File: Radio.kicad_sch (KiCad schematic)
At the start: 3 parts, among them U4 X1000, U5 AP6212

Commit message: Update (Display)
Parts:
- U4: footprint (none) -> TheBrutzlers_Lib:BGA256C80P16X16_1300X1300X130N
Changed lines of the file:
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@@
     (property "Reference" "U4" (id 0) (at 149.86 78.74 0))
     (property "Value" "X1000" (id 1) (at 149.86 81.28 0))
-    (property "Footprint" "" (id 2) (at 153.67 95.25 0)
+    (property "Footprint" "TheBrutzlers_Lib:BGA256C80P16X16_1300X1300X130N" (id 2) (at 153.67 95.25 0)
       (effects (font (size 1.27 1.27)) (justify left) hide)
     )

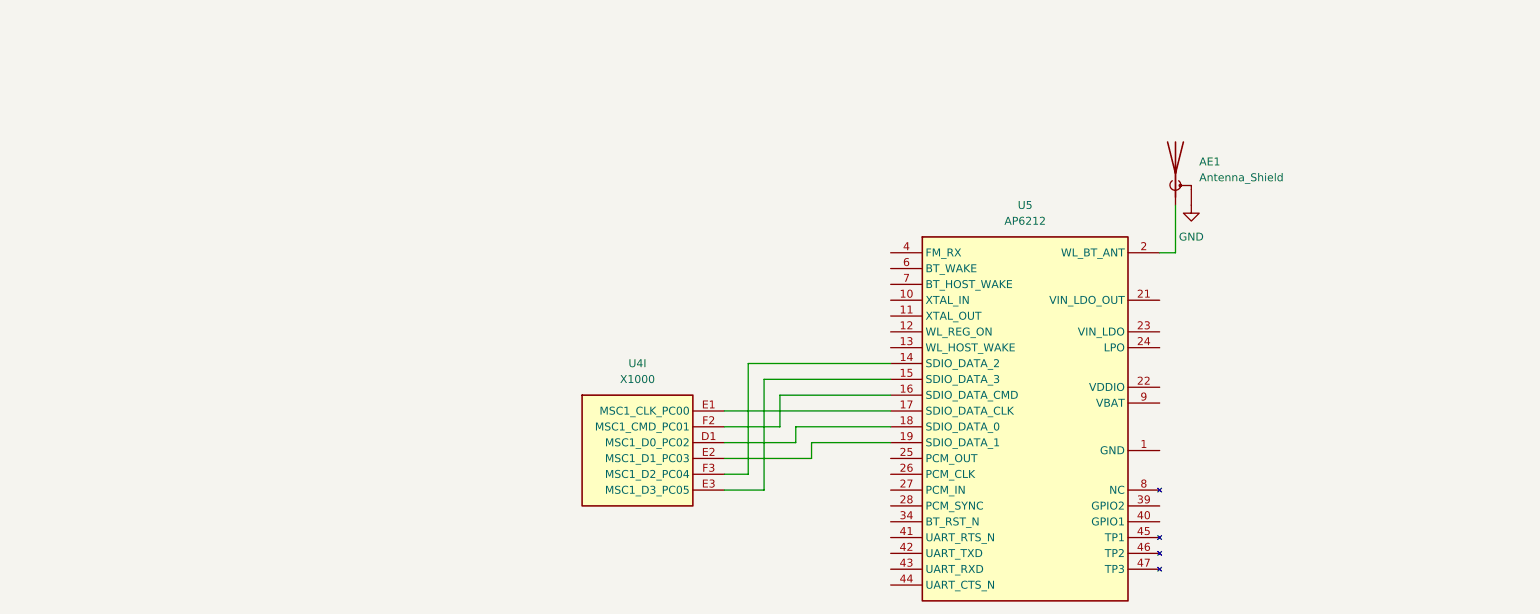
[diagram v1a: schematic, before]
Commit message: Display Update
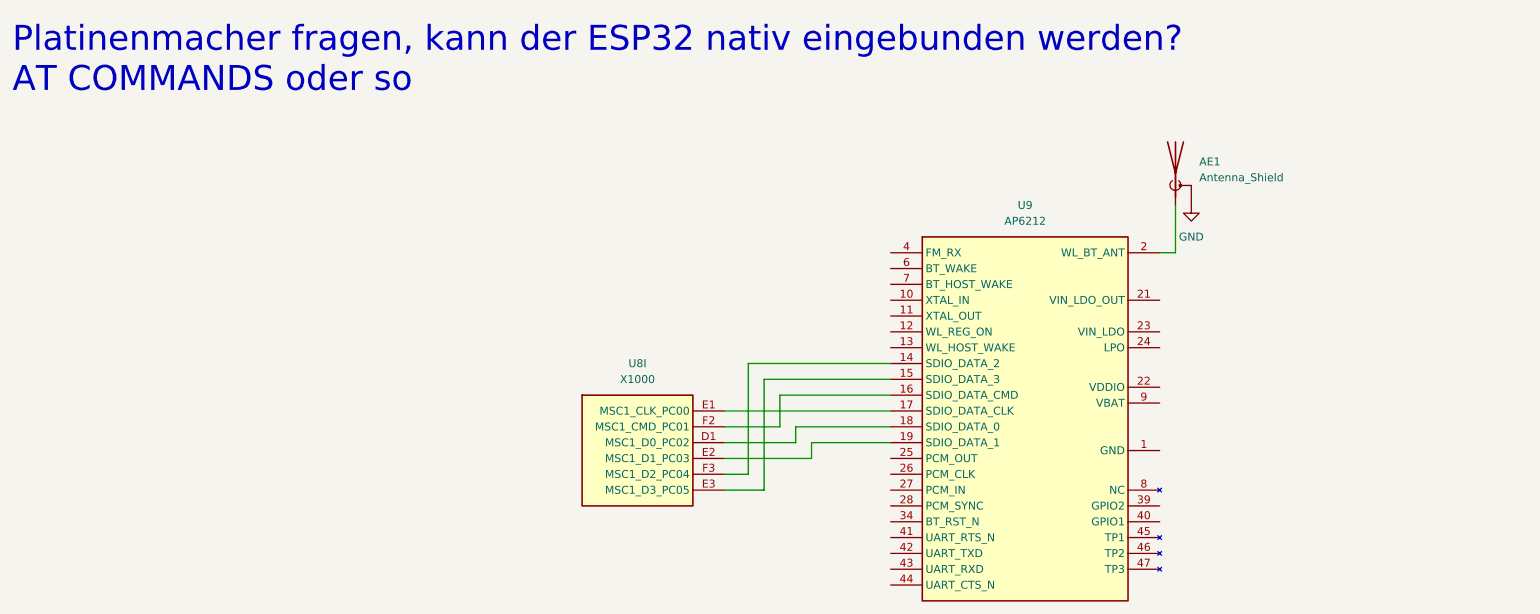
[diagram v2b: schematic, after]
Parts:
- renumbered U4 to U8, U5 to U9
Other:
- note added: "Platinenmacher fragen, kann der ESP32 nativ eingebunden werden? AT COMMANDS oder so"
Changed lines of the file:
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@@
     (stroke (width 0) (type default) (color 0 0 0 0))
+  )
+  (text "Platinenmacher fragen, kann der ESP32 nativ eingebunden werden?\nAT COMMANDS oder so"
+    (at 49.53 35.56 0)
+    (effects (font (size 4 4)) (justify left bottom))
   )
   (symbol (lib_id "TheBrutzlers_Lib:X1000") (at 138.43 85.09 0) (unit 9)
     (in_bom yes) (on_board yes) (fields_autoplaced)
-    (property "Reference" "U4" (id 0) (at 149.86 78.74 0))
+    (property "Reference" "U8" (id 0) (at 149.86 78.74 0))
     (property "Value" "X1000" (id 1) (at 149.86 81.28 0))
     (property "Footprint" "TheBrutzlers_Lib:BGA256C80P16X16_1300X1300X130N" (id 2) (at 153.67 95.25 0)
@@
   (symbol (lib_id "TheBrutzlers_Lib:AP6212") (at 190.5 58.42 0) (unit 1)
     (in_bom yes) (on_board yes) (fields_autoplaced)
-    (property "Reference" "U5" (id 0) (at 212.09 53.34 0))
+    (property "Reference" "U9" (id 0) (at 212.09 53.34 0))
     (property "Value" "AP6212" (id 1) (at 212.09 55.88 0))
     (property "Footprint" "TheBrutzlers_Lib:AP6212" (id 2) (at 195.58 57.15 0)
@@
   (symbol (lib_id "power:GND") (at 238.76 53.34 0) (unit 1)
     (in_bom yes) (on_board yes) (fields_autoplaced)
-    (property "Reference" "#PWR039" (id 0) (at 238.76 59.69 0)
+    (property "Reference" "#PWR048" (id 0) (at 238.76 59.69 0)
       (effects (font (size 1.27 1.27)) hide)
     )

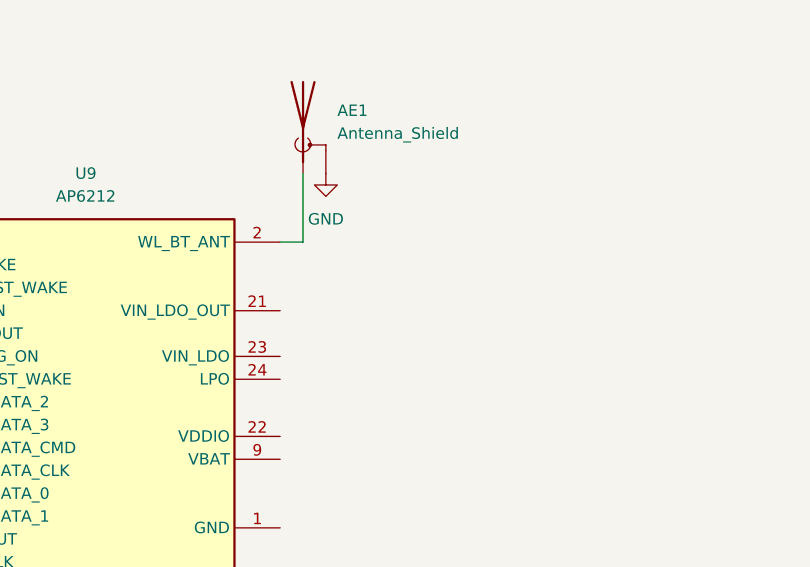
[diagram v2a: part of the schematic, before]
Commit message: update DDR
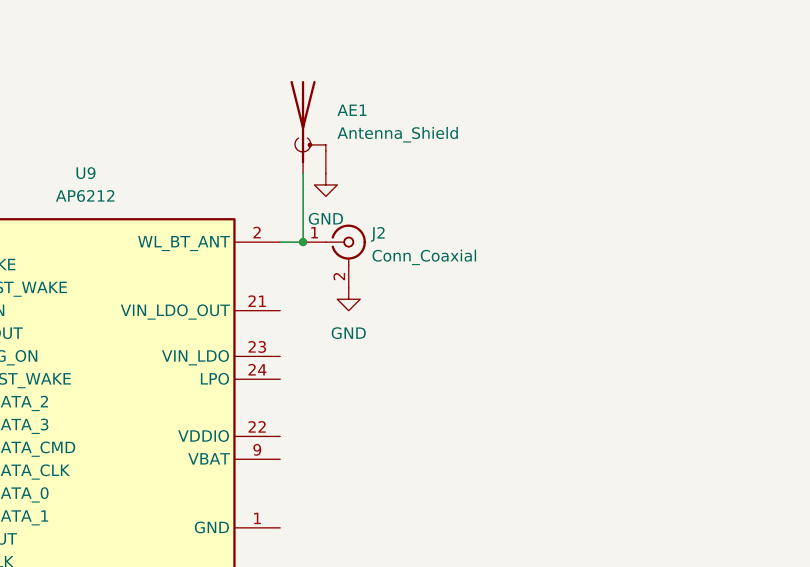
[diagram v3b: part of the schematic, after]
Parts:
- added J2: Conn_Coaxial, Connector_Coaxial:U.FL_Molex_MCRF_73412-0110_Vertical, symbol Connector:Conn_Coaxial
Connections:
- net GND: now also J2.2 (Ext)
- net at AE1.1 (A), U9.2 (WL_BT_ANT): now also J2.1 (In)
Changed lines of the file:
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@@
 (kicad_sch (version 20211123) (generator eeschema)
   (paper "A4")
+  (junction (at 236.22 60.96) (diameter 0) (color 0 0 0 0)
+  )
   (wire (pts (xy 163.83 88.9) (xy 172.72 88.9))
     (stroke (width 0) (type default) (color 0 0 0 0))
@@
   (symbol (lib_id "power:GND") (at 238.76 53.34 0) (unit 1)
     (in_bom yes) (on_board yes) (fields_autoplaced)
-    (property "Reference" "#PWR048" (id 0) (at 238.76 59.69 0)
+    (property "Reference" "#PWR055" (id 0) (at 238.76 59.69 0)
       (effects (font (size 1.27 1.27)) hide)
     )
@@
     (pin "1")
   )
+  (symbol (lib_id "power:GND") (at 241.3 66.04 0) (unit 1)
+    (in_bom yes) (on_board yes) (fields_autoplaced)
+    (property "Reference" "#PWR056" (id 0) (at 241.3 72.39 0)
+      (effects (font (size 1.27 1.27)) hide)
+    )
+    (property "Value" "GND" (id 1) (at 241.3 71.12 0))
+    (property "Footprint" "" (id 2) (at 241.3 66.04 0)
+      (effects (font (size 1.27 1.27)) hide)
+    )
+    (property "Datasheet" "" (id 3) (at 241.3 66.04 0)
+      (effects (font (size 1.27 1.27)) hide)
+    )
+    (pin "1")
+  )
   (symbol (lib_id "Device:Antenna_Shield") (at 236.22 48.26 0) (unit 1)
     (in_bom yes) (on_board yes) (fields_autoplaced)
@@
       (effects (font (size 1.27 1.27)) hide)
     )
+    (pin "1")
+    (pin "2")
+  )
+  (symbol (lib_id "Connector:Conn_Coaxial") (at 241.3 60.96 0) (unit 1)
+    (in_bom yes) (on_board yes) (fields_autoplaced)
+    (property "Reference" "J2" (id 0) (at 243.84 59.9831 0)
+      (effects (font (size 1.27 1.27)) (justify left))
+    )
+    (property "Value" "Conn_Coaxial" (id 1) (at 243.84 62.5231 0)
+      (effects (font (size 1.27 1.27)) (justify left))
+    )
+    (property "Footprint" "Connector_Coaxial:U.FL_Molex_MCRF_73412-0110_Vertical" (id 2) (at 241.3 60.96 0)
+      (effects (font (size 1.27 1.27)) hide)
+    )
+    (property "Datasheet" " ~" (id 3) (at 241.3 60.96 0)
+      (effects (font (size 1.27 1.27)) hide)
+    )
